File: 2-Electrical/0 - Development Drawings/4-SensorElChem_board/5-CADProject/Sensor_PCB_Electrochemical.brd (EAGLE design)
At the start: 55 x 22 mm, 21 parts, among them IC4 LMP91000SD_NOPB, IC5 REF3125AQDBZRQ1, J10 2wire, Q1 PMBFJ177,215, X1 3-ELECTRODE-GAS-SENSOR_SOCKET

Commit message: programing procedure, elchem board
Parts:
- removed FID1, FID2, FID4: FIDUCIAL"", microbuilder:FIDUCIAL_1MM
- removed J10: 2wire, pinhead:1X02
- removed U$1: CONN_03X2_WE_61200621621, FRA_eagle_lib:WE_61200621621
- removed U$2: TGS5042, FRA_eagle_lib:TGS5042
- added C1: DNI, resistor:C0603K
- added DRILEGEND: (no value), drilegend:DRILEGEND
- added FID3, FID5, FID6, FID7, FID8, FID9: FIDUCIAL1X1UNMASKED, microbuilder:FIDUCIAL_1MM_UNMASKED
- added J1: CONN_03X2_WE_61200621621, FRA_eagle_lib:WE_61200621621
- added J2: 2wire, pinhead:1X02
- added JP2: JUMPER-SMT_3_NO_NO_SILK, SparkFun-Jumpers:SMT-JUMPER_3_0-NO_TRACE_NO-SILK
- added U2: TGS5042, FRA_eagle_lib:TGS5042
- moved R21 16.5 mm to (32.1, 14.5)
- moved IC5 15.1 mm to (48.1, 7.38), turned to 270 degrees
- moved C2 14.4 mm to (16.3, 19.8)
- moved C8 11.6 mm to (45.1, 7.55), turned to 270 degrees
- moved LED1 8.99 mm to (24.1, 19.8), turned to 270 degrees
- moved R24 6.49 mm to (24.2, 17.8), turned to 180 degrees
- moved X1 5.91 mm to (35.0, 11.0)
- moved IC4 5.27 mm to (35.0, 11.0)
- moved C12 5.12 mm to (31.1, 8.74)
- moved Q1 4.93 mm to (41.3, 5.81), turned to 0 degrees
- moved R20 4.06 mm to (41.4, 3.08)
- moved R22 2.51 mm to (39.3, 18.6), turned to 90 degrees
- moved R12 1.58 mm to (16.1, 10.8)
- moved C9 0.81 mm to (16.1, 13.5)
- moved FB9 0.38 mm to (16.2, 16.8)
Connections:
- removed net N$19: R22.2, U$2.P$2, U$2.P$3
- new net CE_CO: JP2.1, R22.2, U2.P$2, U2.P$3
- new net N$2: C1.1, IC4.10
- new net N$4: C1.2, IC4.9
- net 5V: now also J1.4; no longer U$1.4
- net 5V_CALM: now also J1.3; no longer U$1.3
- net CE: now also J2.1, JP2.2; no longer J10.1
- net GND: now also J1.1; no longer U$1.1
- net RE: now also J2.2, JP2.3; no longer J10.2
- net SCL: now also J1.6; no longer U$1.6
- net SDA: now also J1.5; no longer U$1.5
- net VOUT: now also J1.2; no longer U$1.2
- net WE: now also U2.P$1; no longer U$2.P$1
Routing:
- net 5V_CALM: track 0.00 -> 79.3 mm, vias 0 -> 3
- net CE_CO: track 0.00 -> 54.5 mm, vias 0 -> 1
- net GND: track 0.00 -> 36.4 mm
- net 5V: track 0.00 -> 32.0 mm, vias 0 -> 1
- net RE: track 0.00 -> 30.1 mm, vias 0 -> 1
- net SDA: track 0.00 -> 28.7 mm
- net N$3: track 0.00 -> 26.1 mm, vias 0 -> 2
- net SCL: track 0.00 -> 24.2 mm
- net WE: track 0.00 -> 21.6 mm
- net CE: track 0.00 -> 17.6 mm
- net VREF: track 0.00 -> 15.0 mm, vias 0 -> 2
- net VOUT: track 0.00 -> 7.62 mm
- net AGND: track 0.00 -> 6.11 mm, vias 0 -> 9
- net N$2: track 0.00 -> 4.69 mm
- net N$4: track 0.00 -> 4.55 mm
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- added copper zone on layer 1, net AGND
- added copper zone on layer 16, net AGND
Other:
- board text added: "El-Chem gas sensor v1"
- board text added: "J. Repcik 08/2019"
- board text added: "short for 2-wire"
- board text added: "short for CO"
- board text removed: "Sensor PCB v1 J.Repcik 7/2019"
- board text removed: "TGS2611 TGS2612 TGS2620"

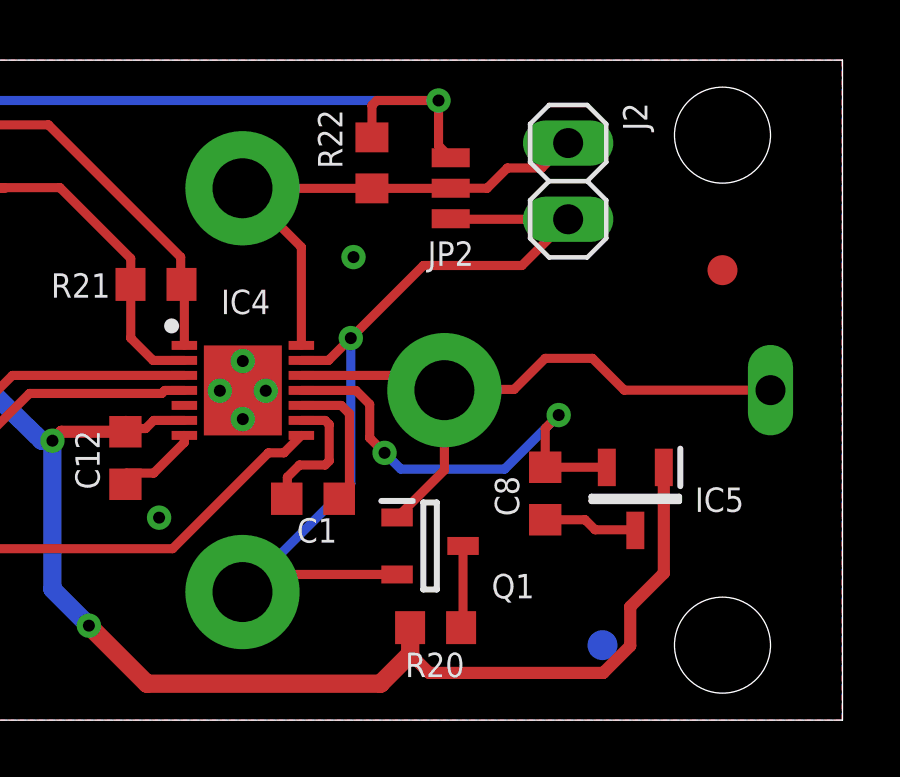
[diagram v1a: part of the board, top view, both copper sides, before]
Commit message: data processing, orders review, tests, elchem pcb RE CE swap
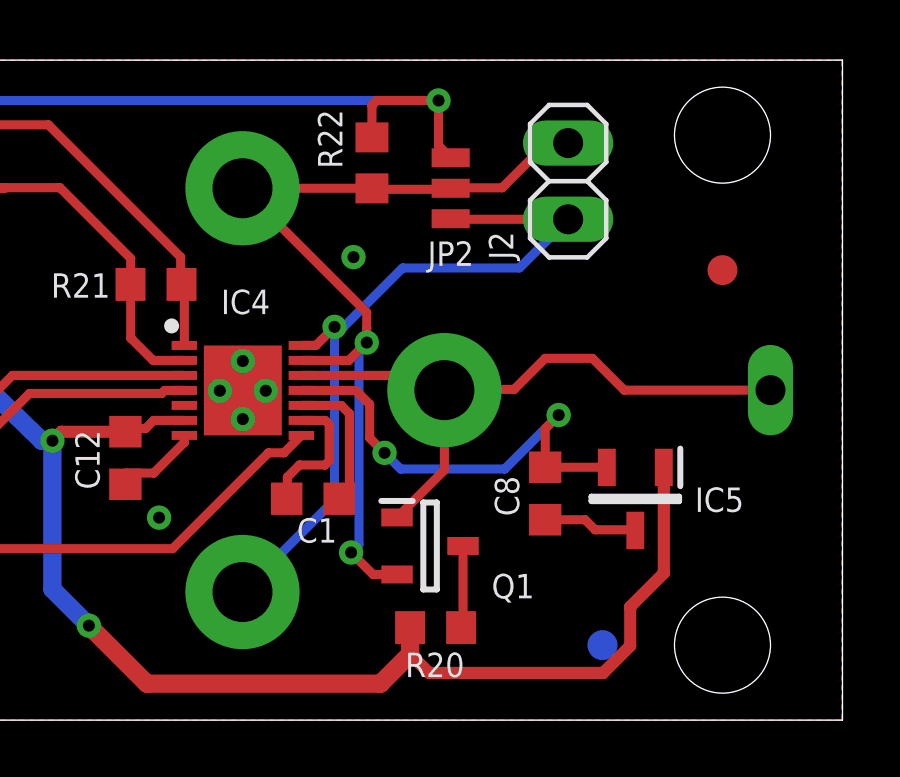
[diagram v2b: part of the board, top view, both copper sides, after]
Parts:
- turned J2 to 90 degrees
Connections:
- net CE_CO renamed RE_CO
- net CE: now also JP2.3; no longer JP2.2, R22.1
- net RE: now also JP2.2, R22.1; no longer JP2.3
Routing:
- net CE: track 17.6 -> 24.7 mm, vias 0 -> 1
- net RE: track 30.1 -> 29.8 mm, vias 1 -> 2
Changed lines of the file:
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@@
 <grid distance="0.0307" unitdist="mm" unit="mm" style="lines" multiple="1" display="yes" altdistance="0.0635" altunitdist="mm" altunit="mm"/>
 <layers>
-<layer number="1" name="Top" color="4" fill="1" visible="no" active="yes"/>
+<layer number="1" name="Top" color="4" fill="1" visible="yes" active="yes"/>
 <layer number="2" name="Route2" color="1" fill="3" visible="no" active="no"/>
 <layer number="3" name="Route3" color="4" fill="3" visible="no" active="no"/>
@@
 <layer number="19" name="Unrouted" color="6" fill="1" visible="yes" active="yes"/>
 <layer number="20" name="Dimension" color="15" fill="1" visible="yes" active="yes"/>
-<layer number="21" name="tPlace" color="7" fill="1" visible="no" active="yes"/>
+<layer number="21" name="tPlace" color="7" fill="1" visible="yes" active="yes"/>
 <layer number="22" name="bPlace" color="7" fill="1" visible="yes" active="yes"/>
-<layer number="23" name="tOrigins" color="15" fill="1" visible="no" active="yes"/>
-<layer number="24" name="bOrigins" color="15" fill="1" visible="no" active="yes"/>
+<layer number="23" name="tOrigins" color="15" fill="1" visible="yes" active="yes"/>
+<layer number="24" name="bOrigins" color="15" fill="1" visible="yes" active="yes"/>
 <layer number="25" name="tNames" color="7" fill="1" visible="no" active="yes"/>
 <layer number="26" name="bNames" color="7" fill="1" visible="yes" active="yes"/>
@@
 <attribute name="VALUE" x="17.947" y="16.047" size="0.4064" layer="27" font="vector" ratio="10"/>
 </element>
-<element name="J2" library="pinhead" package="1X02" value="2wire" x="45.855" y="17.966" smashed="yes" rot="R270">
-<attribute name="PARTNO" value="TSW-102-07-G-S" x="41.029" y="17.966" size="1.778" layer="27" rot="R270" display="off"/>
-<attribute name="NAME" x="47.6838" y="20.5822" size="0.8128" layer="25" ratio="10" rot="R270"/>
-<attribute name="VALUE" x="42.68" y="20.506" size="1.27" layer="27" rot="R270"/>
+<element name="J2" library="pinhead" package="1X02" value="2wire" x="45.855" y="17.966" smashed="yes" rot="R90">
+<attribute name="PARTNO" value="TSW-102-07-G-S" x="50.681" y="17.966" size="1.778" layer="27" rot="R90" display="off"/>
+<attribute name="NAME" x="44.0262" y="15.3498" size="0.8128" layer="25" ratio="10" rot="R90"/>
+<attribute name="VALUE" x="49.03" y="15.426" size="1.27" layer="27" rot="R90"/>
 </element>
 <element name="IC4" library="SamacSys_Parts" package="SON50P400X400X80-15N" value="LMP91000SD_NOPB" x="35.012" y="10.991" smashed="yes">
@@
 </signal>
 <signal name="RE">
-<contactref element="X1" pad="R"/>
 <contactref element="IC4" pad="13"/>
 <contactref element="Q1" pad="2"/>
 <contactref element="J2" pad="2"/>
-<wire x1="36.962" y1="11.991" x2="37.866" y2="11.991" width="0.3048" layer="1"/>
-<wire x1="37.866" y1="11.991" x2="38.61" y2="12.735" width="0.3048" layer="1"/>
-<via x="38.61" y="12.735" extent="1-16" drill="0.4" diameter="0.8128"/>
-<wire x1="38.61" y1="12.735" x2="38.61" y2="7.88" width="0.3048" layer="16"/>
-<wire x1="38.61" y1="7.88" x2="35" y2="4.27" width="0.3048" layer="16"/>
-<wire x1="40.152" y1="4.856" x2="35.586" y2="4.856" width="0.3048" layer="1"/>
-<wire x1="35.586" y1="4.856" x2="35" y2="4.27" width="0.3048" layer="1"/>
-<wire x1="38.61" y1="12.735" x2="41.03" y2="15.155" width="0.3048" layer="1"/>
-<wire x1="45.855" y1="16.696" x2="44.314" y2="15.155" width="0.3048" layer="1"/>
-<contactref element="JP2" pad="3"/>
-<wire x1="41.03" y1="15.155" x2="44.314" y2="15.155" width="0.3048" layer="1"/>
-<wire x1="41.94" y1="16.714" x2="41.958" y2="16.696" width="0.3048" layer="1"/>
-<wire x1="41.958" y1="16.696" x2="45.855" y2="16.696" width="0.3048" layer="1"/>
-</signal>
-<signal name="CE">
-<contactref element="X1" pad="C"/>
-<contactref element="IC4" pad="14"/>
-<contactref element="J2" pad="1"/>
+<wire x1="36.962" y1="11.991" x2="38.5465" y2="11.991" width="0.3048" layer="1"/>
 <contactref element="R22" pad="1"/>
-<wire x1="36.962" y1="12.491" x2="36.962" y2="15.768" width="0.3048" layer="1"/>
-<wire x1="36.962" y1="15.768" x2="35.004" y2="17.726" width="0.3048" layer="1"/>
-<wire x1="39.315" y1="17.726" x2="35.004" y2="17.726" width="0.3048" layer="1"/>
-<wire x1="35.004" y1="17.726" x2="35" y2="17.73" width="0.3048" layer="1"/>
-<wire x1="45.831" y1="19.26" x2="45.855" y2="19.236" width="0.3048" layer="1"/>
 <wire x1="39.315" y1="17.726" x2="39.346" y2="17.695" width="0.3048" layer="1"/>
 <contactref element="JP2" pad="2"/>
 <wire x1="41.94" y1="17.73" x2="41.936" y2="17.726" width="0.3048" layer="1"/>
-<wire x1="41.936" y1="17.726" x2="39.315" y2="17.726" width="0.3048" layer="1"/>
-<wire x1="45.831" y1="19.26" x2="44.976" y2="18.405" width="0.3048" layer="1"/>
-<wire x1="44.976" y1="18.405" x2="43.83" y2="18.405" width="0.3048" layer="1"/>
-<wire x1="43.83" y1="18.405" x2="43.155" y2="17.73" width="0.3048" layer="1"/>
-<wire x1="43.155" y1="17.73" x2="41.94" y2="17.73" width="0.3048" layer="1"/>
+<contactref element="X1" pad="R"/>
+<wire x1="35" y1="17.73" x2="39.311" y2="17.73" width="0.3048" layer="1"/>
+<wire x1="39.311" y1="17.73" x2="39.315" y2="17.726" width="0.3048" layer="1"/>
+<wire x1="39.346" y1="17.695" x2="41.905" y2="17.695" width="0.3048" layer="1"/>
+<wire x1="41.905" y1="17.695" x2="41.94" y2="17.73" width="0.3048" layer="1"/>
+<wire x1="39.1425" y1="13.5875" x2="35" y2="17.73" width="0.3048" layer="1"/>
+<wire x1="43.6554" y1="17.7446" x2="41.9546" y2="17.7446" width="0.3048" layer="1"/>
+<wire x1="41.9546" y1="17.7446" x2="41.94" y2="17.73" width="0.3048" layer="1"/>
+<wire x1="45.855" y1="19.236" x2="45.1468" y2="19.236" width="0.3048" layer="1"/>
+<wire x1="45.1468" y1="19.236" x2="43.6554" y2="17.7446" width="0.3048" layer="1"/>
+<wire x1="38.5465" y1="11.991" x2="39.1425" y2="12.587" width="0.3048" layer="1"/>
+<wire x1="39.1425" y1="13.0782" x2="39.1425" y2="13.5875" width="0.3048" layer="1"/>
+<wire x1="40.152" y1="4.856" x2="39.352" y2="4.856" width="0.3048" layer="1"/>
+<wire x1="39.352" y1="4.856" x2="38.6206" y2="5.5874" width="0.3048" layer="1"/>
+<via x="38.6206" y="5.5874" extent="1-16" drill="0.4" diameter="0.8128"/>
+<wire x1="38.6206" y1="5.5874" x2="38.88155" y2="5.84835" width="0.3048" layer="16"/>
+<wire x1="38.88155" y1="5.84835" x2="38.88155" y2="12.32605" width="0.3048" layer="16"/>
+<wire x1="38.88155" y1="12.32605" x2="39.1425" y2="12.587" width="0.3048" layer="16"/>
+<via x="39.1425" y="12.587" extent="1-16" drill="0.4" diameter="0.8128"/>
+<wire x1="39.1425" y1="12.587" x2="39.1425" y2="13.0782" width="0.3048" layer="1"/>
+</signal>
+<signal name="CE">
+<contactref element="IC4" pad="14"/>
+<contactref element="J2" pad="1"/>
+<contactref element="JP2" pad="3"/>
+<contactref element="X1" pad="C"/>
+<wire x1="45.855" y1="16.696" x2="41.958" y2="16.696" width="0.3048" layer="1"/>
+<wire x1="41.958" y1="16.696" x2="41.94" y2="16.714" width="0.3048" layer="1"/>
+<wire x1="36.962" y1="12.491" x2="37.4501" y2="12.491" width="0.3048" layer="1"/>
+<wire x1="37.4501" y1="12.491" x2="38.068" y2="13.1089" width="0.3048" layer="1"/>
+<via x="38.068" y="13.1089" extent="1-16" drill="0.4" diameter="0.8128"/>
+<wire x1="38.068" y1="13.1089" x2="38.068" y2="7.338" width="0.3048" layer="16"/>
+<wire x1="38.068" y1="7.338" x2="35" y2="4.27" width="0.3048" layer="16"/>
+<wire x1="38.068" y1="13.1089" x2="38.375" y2="13.1089" width="0.3048" layer="16"/>
+<wire x1="38.375" y1="13.1089" x2="40.3398" y2="15.0737" width="0.3048" layer="16"/>
+<wire x1="40.3398" y1="15.0737" x2="44.2327" y2="15.0737" width="0.3048" layer="16"/>
+<wire x1="44.2327" y1="15.0737" x2="45.855" y2="16.696" width="0.3048" layer="16"/>
 </signal>
 <signal name="VREF">
@@
 <wire x1="42.352" y1="3.149" x2="42.287" y2="3.084" width="0.3048" layer="1"/>
 </signal>
-<signal name="CE_CO">
-<contactref element="R22" pad="2"/>
-<contactref element="U2" pad="P$3"/>
-<contactref element="U2" pad="P$2"/>
-<wire x1="39.315" y1="19.426" x2="39.315" y2="20.49" width="0.3048" layer="1"/>
-<wire x1="2.4" y1="14.75" x2="4.22" y2="14.75" width="0.3048" layer="16"/>
-<wire x1="4.22" y1="14.75" x2="10.125" y2="20.655" width="0.3048" layer="16"/>
-<via x="41.535" y="20.655" extent="1-16" drill="0.4" diameter="0.8128"/>
-<wire x1="41.535" y1="20.655" x2="39.48" y2="20.655" width="0.3048" layer="1"/>
-<wire x1="39.48" y1="20.655" x2="39.315" y2="20.49" width="0.3048" layer="1"/>
-<wire x1="10.125" y1="20.655" x2="41.535" y2="20.655" width="0.3048" layer="16"/>
-<contactref element="JP2" pad="1"/>
-<wire x1="41.94" y1="18.746" x2="41.535" y2="19.151" width="0.3048" layer="1"/>
-<wire x1="41.535" y1="19.151" x2="41.535" y2="20.655" width="0.3048" layer="1"/>
-<wire x1="2.4" y1="14.75" x2="2.4" y2="7.25" width="0.254" layer="16"/>
-</signal>
 <signal name="N$1">
 <contactref element="R24" pad="2"/>
@@
 <wire x1="36.495" y1="7.4" x2="36.475" y2="7.38" width="0.3048" layer="1"/>
 </signal>
+<signal name="RE_CO">
+<contactref element="JP2" pad="1"/>
+<contactref element="R22" pad="2"/>
+<contactref element="U2" pad="P$3"/>
+<contactref element="U2" pad="P$2"/>
+<wire x1="39.315" y1="19.426" x2="39.315" y2="20.49" width="0.3048" layer="1"/>
+<wire x1="2.4" y1="14.75" x2="4.22" y2="14.75" width="0.3048" layer="16"/>
+<wire x1="4.22" y1="14.75" x2="10.125" y2="20.655" width="0.3048" layer="16"/>
+<via x="41.535" y="20.655" extent="1-16" drill="0.4" diameter="0.8128"/>
+<wire x1="41.535" y1="20.655" x2="39.48" y2="20.655" width="0.3048" layer="1"/>
+<wire x1="39.48" y1="20.655" x2="39.315" y2="20.49" width="0.3048" layer="1"/>
+<wire x1="10.125" y1="20.655" x2="41.535" y2="20.655" width="0.3048" layer="16"/>
+<wire x1="41.535" y1="19.151" x2="41.535" y2="20.655" width="0.3048" layer="1"/>
+<wire x1="2.4" y1="14.75" x2="2.4" y2="7.25" width="0.254" layer="16"/>
+<wire x1="41.535" y1="19.151" x2="41.94" y2="18.746" width="0.3048" layer="1"/>
+</signal>
 </signals>
